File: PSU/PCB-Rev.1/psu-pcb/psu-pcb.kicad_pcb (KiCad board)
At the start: 2 copper layers, 100 x 100 mm, 60 parts, among them J1 Conn_02x07_Odd_Even, J2 OSTTC022162, J3 OSTTC022162, J4 OSTTC022162, J5 OSTTC022162, J6 OSTTC022162, J7 OSTTC022162, J8 Conn_02x05_Odd_Even, Q1 2N7002, Q2 2N7002, Q3 2N7002, Q4 FQP27P06, Q5 2N7002, U1 PIC12F1501-IP, U2 ADS1110

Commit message: psu ready to be validated
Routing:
- net +12V: track 135.8 -> 119.2 mm
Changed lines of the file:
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@@
-(kicad_pcb (version 20171130) (host pcbnew 5.0.2+dfsg1-1~bpo9+1)
+(kicad_pcb (version 20171130) (host pcbnew "(5.1.5)-3")
   (general
     (thickness 1.6)
     (drawings 6)
-    (tracks 213)
+    (tracks 211)
     (zones 0)
     (modules 60)
@@
     (38 B.Mask user)
     (39 F.Mask user)
-    (40 Dwgs.User user)
-    (41 Cmts.User user)
-    (42 Eco1.User user)
-    (43 Eco2.User user)
+    (40 Dwgs.User user hide)
+    (41 Cmts.User user hide)
+    (42 Eco1.User user hide)
+    (43 Eco2.User user hide)
     (44 Edge.Cuts user)
     (45 Margin user)
     (46 B.CrtYd user)
     (47 F.CrtYd user)
-    (48 B.Fab user)
-    (49 F.Fab user)
+    (48 B.Fab user hide)
+    (49 F.Fab user hide)
   )
   (setup
-    (last_trace_width 0.25)
+    (last_trace_width 2.54)
     (user_trace_width 1.27)
     (user_trace_width 2.54)
@@
     (zone_45_only no)
     (trace_min 0.2)
-    (segment_width 0.2)
-    (edge_width 0.15)
     (via_size 0.8)
     (via_drill 0.4)
@@
     (uvia_min_size 0.2)
     (uvia_min_drill 0.1)
+    (edge_width 0.15)
+    (segment_width 0.2)
     (pcb_text_width 0.3)
     (pcb_text_size 1.5 1.5)
@@
     (solder_mask_min_width 0.25)
     (aux_axis_origin 0 0)
-    (visible_elements FFFFFF7F)
+    (visible_elements 7FFFFFFF)
     (pcbplotparams
       (layerselection 0x010fc_ffffffff)
@@
   (gr_line (start 120 120) (end 120 20) (layer Edge.Cuts) (width 0.01))
   (gr_line (start 20 20) (end 20 120) (layer Edge.Cuts) (width 0.01))
-  (via (at 116.84 22.86) (size 3.81) (drill 2.54) (layers F.Cu B.Cu) (net 2))
-  (via (at 36.83 83.185) (size 0.8) (drill 0.4) (layers F.Cu B.Cu) (net 2))
-  (via (at 42.545 53.34) (size 0.8) (drill 0.4) (layers F.Cu B.Cu) (net 2))
   (segment (start 38.735 33.655) (end 34.925 29.845) (width 2.54) (layer F.Cu) (net 1))
   (segment (start 41.275 33.655) (end 38.735 33.655) (width 2.54) (layer F.Cu) (net 1))
   (segment (start 28.575 36.195) (end 34.925 29.845) (width 2.54) (layer B.Cu) (net 1))
   (segment (start 26.035 36.195) (end 28.575 36.195) (width 2.54) (layer B.Cu) (net 1))
+  (via (at 116.84 22.86) (size 3.81) (drill 2.54) (layers F.Cu B.Cu) (net 2))
+  (via (at 36.83 83.185) (size 0.8) (drill 0.4) (layers F.Cu B.Cu) (net 2))
+  (via (at 42.545 53.34) (size 0.8) (drill 0.4) (layers F.Cu B.Cu) (net 2))
   (segment (start 66.04 36.8) (end 66.04 35.56) (width 0.25) (layer F.Cu) (net 2))
   (segment (start 62.865 39.975) (end 66.04 36.8) (width 0.25) (layer F.Cu) (net 2))
@@
   (segment (start 63.915 55.025) (end 63.5 54.61) (width 0.25) (layer F.Cu) (net 8))
   (segment (start 63.915 60.96) (end 63.915 55.025) (width 0.25) (layer F.Cu) (net 8))
-  (segment (start 68.780001 76.079999) (end 69.93 74.93) (width 6.35) (layer B.Cu) (net 9))
-  (segment (start 62.865 81.995) (end 68.780001 76.079999) (width 6.35) (layer B.Cu) (net 9))
-  (segment (start 62.865 91.36) (end 62.865 81.995) (width 6.35) (layer B.Cu) (net 9))
-  (segment (start 65.485 93.98) (end 62.865 91.36) (width 6.35) (layer B.Cu) (net 9))
-  (segment (start 69.93 74.93) (end 54.69 59.69) (width 6.35) (layer B.Cu) (net 9))
   (segment (start 44.875 28.745) (end 47.625 25.995) (width 2.54) (layer F.Cu) (net 9))
   (segment (start 44.875 33.655) (end 44.875 28.745) (width 2.54) (layer F.Cu) (net 9))
@@
   (segment (start 64.135 52.705) (end 66.04 54.61) (width 0.25) (layer F.Cu) (net 9))
   (segment (start 59.055 52.705) (end 64.135 52.705) (width 0.25) (layer F.Cu) (net 9))
-  (segment (start 63.701002 50.165) (end 54.69 50.165) (width 2.54) (layer B.Cu) (net 9))
-  (segment (start 66.04 52.503998) (end 63.701002 50.165) (width 2.54) (layer B.Cu) (net 9))
-  (segment (start 66.04 54.61) (end 66.04 52.503998) (width 2.54) (layer B.Cu) (net 9))
-  (segment (start 54.69 59.69) (end 54.69 50.165) (width 6.35) (layer B.Cu) (net 9))
-  (segment (start 54.69 50.165) (end 54.69 25.4) (width 6.35) (layer B.Cu) (net 9))
+  (segment (start 66.04 36.75) (end 66.04 54.61) (width 2.54) (layer B.Cu) (net 9))
+  (segment (start 54.69 25.4) (end 66.04 36.75) (width 2.54) (layer B.Cu) (net 9))
+  (segment (start 66.04 71.04) (end 69.93 74.93) (width 2.54) (layer B.Cu) (net 9))
+  (segment (start 66.04 54.61) (end 66.04 71.04) (width 2.54) (layer B.Cu) (net 9))
+  (segment (start 65.445 79.415) (end 65.445 83.185) (width 2.54) (layer B.Cu) (net 9))
+  (segment (start 69.93 74.93) (end 65.445 79.415) (width 2.54) (layer B.Cu) (net 9))
+  (segment (start 65.445 93.94) (end 65.485 93.98) (width 2.54) (layer B.Cu) (net 9))
+  (segment (start 65.445 83.185) (end 65.445 93.94) (width 2.54) (layer B.Cu) (net 9))
   (segment (start 83.265 54.61) (end 76.835 54.61) (width 2.54) (layer F.Cu) (net 10))
   (segment (start 83.9 55.245) (end 83.265 54.61) (width 2.54) (layer F.Cu) (net 10))

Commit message: update
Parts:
- added G***: LOGO, cidco:logo cidco, F.Cu at (48.3, 78.1)
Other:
- board text removed: "CIDCO.CA Poseidon PSU"

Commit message: update psu and hat
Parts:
- moved R14 31.4 mm to (89.2, 57.1)
- moved Q5 29.8 mm to (92.7, 61.0)
- moved R15 29.7 mm to (96.2, 57.8), turned to 180 degrees
- moved Q4 29.2 mm to (92.7, 53.3)
- moved R11 26.7 mm to (79.4, 59.7), turned to 90 degrees
- moved Q1 26.1 mm to (83.2, 61.6)
- moved C12 11.6 mm to (85.1, 53.3), turned to 90 degrees
- moved L4 11.0 mm to (75.6, 53.3)
- moved C11 10.9 mm to (66.0, 53.4)
- moved J7 6.38 mm to (61.6, 108.0)
- moved G*** 4.58 mm to (45.7, 81.9)
- moved C1 4.45 mm to (52.1, 43.5)
- moved D1 4.45 mm to (39.4, 29.8)
- moved D2 4.45 mm to (55.9, 37.2)
- moved F1 4.45 mm to (47.5, 33.7)
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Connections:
- C11 pad 1: Net-(C11-Pad1) -> +12V
- D3 pad 1: Net-(C12-Pad1) -> Net-(D3-Pad1)
- J4 pad 2: Net-(C12-Pad1) -> Net-(D3-Pad1)
- J8 pad 10: Net-(J8-Pad10) -> (no net)
- J8 pad 2: Net-(J8-Pad2) -> (no net)
- J8 pad 4: Net-(J8-Pad4) -> (no net)
- J8 pad 6: Net-(J8-Pad6) -> (no net)
- J8 pad 8: Net-(J8-Pad8) -> (no net)
- L4 pad 2: Net-(C11-Pad1) -> +12V
- Q4 pad 2: +12V -> Net-(C12-Pad1)
- Q4 pad 3: Net-(C11-Pad1) -> Net-(D3-Pad1)
- R14 pad 1: +12V -> Net-(C12-Pad1)
- R15 pad 1: +12V -> Net-(C12-Pad1)
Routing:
- net GND: track 28.6 -> 51.7 mm, vias 8 -> 7
- net Net-(C11-Pad1): track 15.6 -> 0.00 mm
- net Net-(D3-Pad1): track 0.00 -> 13.5 mm
- net Net-(C12-Pad1): track 24.7 -> 32.8 mm
- net 5v_on: track 61.9 -> 55.0 mm
- net Net-(C5-Pad1): track 54.9 -> 52.4 mm
- net SDA: track 47.7 -> 50.2 mm
- net Net-(D1-Pad1): track 19.4 -> 21.9 mm
- net +12V: track 119.2 -> 121.3 mm
- net read_sw: track 35.9 -> 33.9 mm
- net SCK: track 44.3 -> 46.1 mm
- net Net-(PS1-Pad1): track 9.57 -> 7.97 mm
- net 12v_on: track 71.7 -> 73.2 mm, vias 0 -> 1
- net Net-(PS1-Pad5): track 26.2 -> 24.9 mm
- net +5V: track 151.6 -> 150.6 mm
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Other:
- board text added: "+ -"
- board text added: "12V IN"
- board text added: "12V OUT"
- board text added: "24V OUT"
- board text added: "3.3V OUT"
- board text added: "5V OUT"
- board text added: "DD20200127 Rev. 1.0"
- board text added: "Hydro B. HAT"
- board text added: "Hydro B. PSU"
- board text added: "ICSP"
- board text added: "Read Switch"
- board text removed: "DD200127 Rev. 1.0"

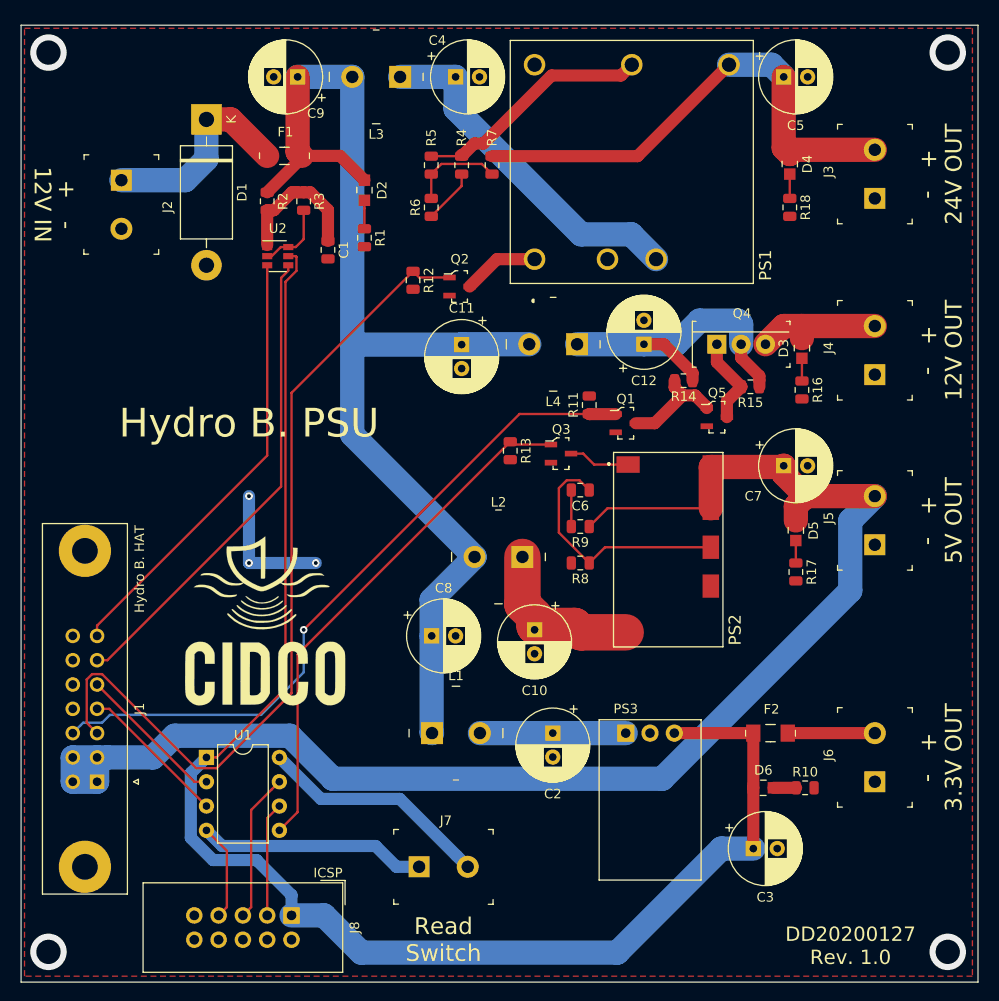
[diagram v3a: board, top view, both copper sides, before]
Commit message: smt to TH
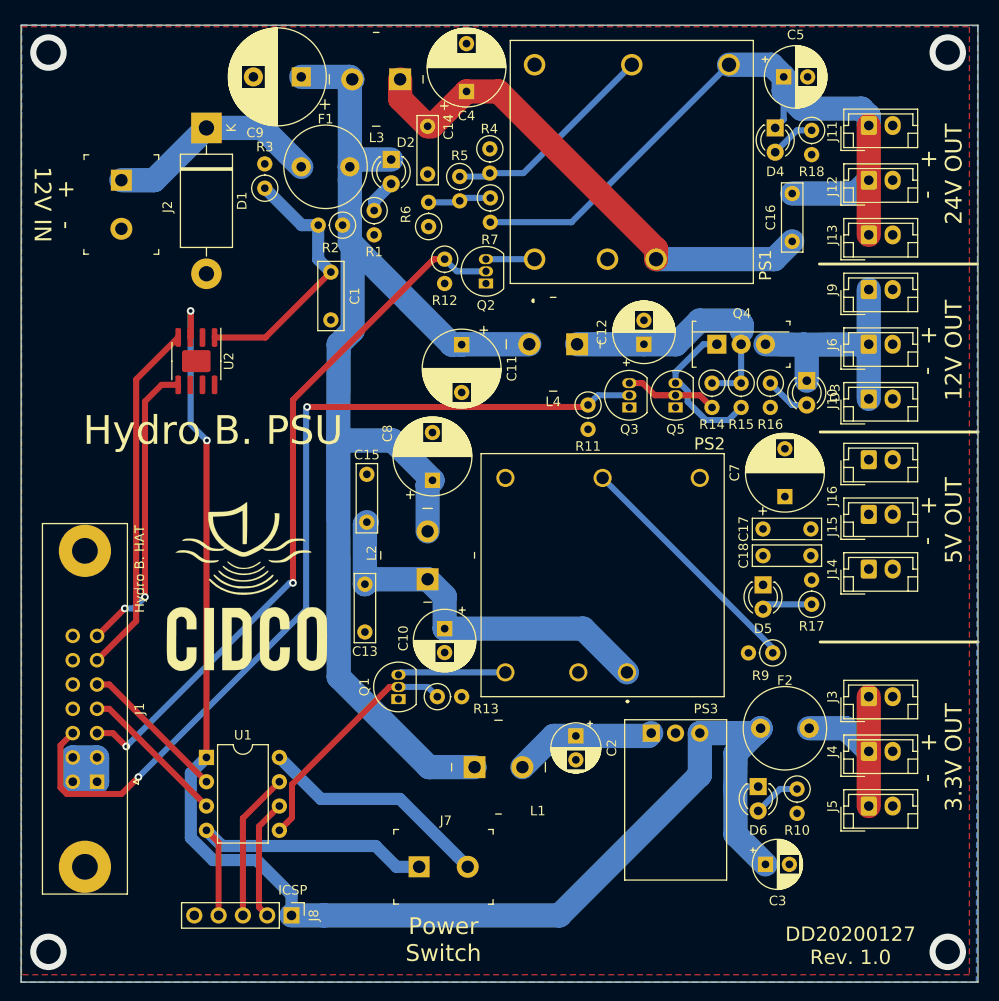
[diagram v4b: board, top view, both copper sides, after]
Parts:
- removed C6: C, Capacitor_SMD:C_0805_2012Metric
- removed R8: R_US, Resistor_SMD:R_0805_2012Metric
- added C13: 10UF, Capacitor_THT:C_Rect_L7.0mm_W2.0mm_P5.00mm, F.Cu at (55.9, 78.4)
- added C14: 4.7UF 50V, Capacitor_THT:C_Rect_L7.0mm_W2.0mm_P5.00mm, F.Cu at (62.5, 30.6)
- added C15: 0.1UF, Capacitor_THT:C_Rect_L7.0mm_W2.0mm_P5.00mm, F.Cu at (56.1, 71.9)
- added C16: 1NF 2KV, Capacitor_THT:C_Rect_L7.0mm_W2.0mm_P5.00mm, F.Cu at (100.6, 42.6)
- added C17: 10UF, Capacitor_THT:C_Rect_L7.0mm_W2.0mm_P5.00mm, F.Cu at (97.5, 72.6)
- added C18: 0.1UF, Capacitor_THT:C_Rect_L7.0mm_W2.0mm_P5.00mm, F.Cu at (97.5, 75.4)
- added J10: Conn_01x02, Connector_JST:JST_EH_B2B-EH-A_1x02_P2.50mm_Vertical, F.Cu at (108.6, 59.1)
- added J11: Conn_01x02, Connector_JST:JST_EH_B2B-EH-A_1x02_P2.50mm_Vertical, F.Cu at (108.6, 30.5)
- added J12: Conn_01x02, Connector_JST:JST_EH_B2B-EH-A_1x02_P2.50mm_Vertical, F.Cu at (108.6, 36.2)
- added J13: Conn_01x02, Connector_JST:JST_EH_B2B-EH-A_1x02_P2.50mm_Vertical, F.Cu at (108.6, 41.9)
- added J14: Conn_01x02, Connector_JST:JST_EH_B2B-EH-A_1x02_P2.50mm_Vertical, F.Cu at (108.6, 76.8)
- added J15: Conn_01x02, Connector_JST:JST_EH_B2B-EH-A_1x02_P2.50mm_Vertical, F.Cu at (108.6, 71.1)
- added J16: Conn_01x02, Connector_JST:JST_EH_B2B-EH-A_1x02_P2.50mm_Vertical, F.Cu at (108.6, 65.4)
- added J9: Conn_01x02, Connector_JST:JST_EH_B2B-EH-A_1x02_P2.50mm_Vertical, F.Cu at (108.6, 47.6)
- C1: value C -> 0.1u; footprint Capacitor_SMD:C_0805_2012Metric -> Capacitor_THT:C_Rect_L7.0mm_W2.5mm_P5.00mm
- C10: value CP1 -> 47UF 35V; footprint Capacitor_THT:CP_Radial_D7.5mm_P2.50mm -> Capacitor_THT:CP_Radial_D6.3mm_P2.50mm
- C11, C4: value CP1 -> 100UF 50V; footprint Capacitor_THT:CP_Radial_D7.5mm_P2.50mm -> Capacitor_THT:CP_Radial_D8.0mm_P5.00mm
- C12, C5: value CP1 -> 47UF 50V; footprint Capacitor_THT:CP_Radial_D7.5mm_P2.50mm -> Capacitor_THT:CP_Radial_D6.3mm_P2.50mm
- C2: value CP1 -> 10u 35v; footprint Capacitor_THT:CP_Radial_D7.5mm_P2.50mm -> Capacitor_THT:CP_Radial_D5.0mm_P2.50mm
- C3: value CP1 -> 10u 10v; footprint Capacitor_THT:CP_Radial_D7.5mm_P2.50mm -> Capacitor_THT:CP_Radial_D5.0mm_P2.50mm
- C7: value CP1 -> 330uf 16v; footprint Capacitor_THT:CP_Radial_D7.5mm_P2.50mm -> Capacitor_THT:CP_Radial_D8.0mm_P5.00mm
- C8: value CP1 -> 100UF 35V; footprint Capacitor_THT:CP_Radial_D7.5mm_P2.50mm -> Capacitor_THT:CP_Radial_D8.0mm_P5.00mm
- C9: value CP1 -> 330UF 50V; footprint Capacitor_THT:CP_Radial_D7.5mm_P2.50mm -> Capacitor_THT:CP_Radial_D10.0mm_P5.00mm
- D2, D3, D4, D5, D6: footprint digikey-footprints:0805 -> LED_THT:LED_D3.0mm_Clear
- F1, F2: footprint digikey-footprints:1206 -> Fuse:Fuse_Littelfuse_372_D8.50mm
- J3, J4, J5, J6: value OSTTC022162 -> Conn_01x02; footprint digikey-footprints:Term_Block_1x2_P5.08MM -> Connector_JST:JST_EH_B2B-EH-A_1x02_P2.50mm_Vertical
- J8: value Conn_02x05_Odd_Even -> Conn_01x05; footprint Connector_IDC:IDC-Header_2x05_P2.54mm_Vertical -> Connector_PinHeader_2.54mm:PinHeader_1x05_P2.54mm_Vertical
- L1: value 13R106C -> 1uh
- L3: value 13R106C -> 2.2UH 4A
- L4: value 13R106C -> 1UH
- PS2: value APXW005A0X3-SRZ -> SKMW30F-05; footprint APXW005A0X3SRZ -> SKMW30G-12:SKMW30G12
- Q1, Q2, Q3, Q5: value 2N7002 -> 2N7000; footprint digikey-footprints:SOT-23-3 -> Package_TO_SOT_THT:TO-92_Inline
- R1, R14, R15: value R_US -> 10k; footprint Resistor_SMD:R_0805_2012Metric -> Resistor_THT:R_Axial_DIN0207_L6.3mm_D2.5mm_P2.54mm_Vertical
- R10: value R_US -> 220; footprint Resistor_SMD:R_0805_2012Metric -> Resistor_THT:R_Axial_DIN0207_L6.3mm_D2.5mm_P2.54mm_Vertical
- R11, R12, R13: value R_US -> 1k; footprint Resistor_SMD:R_0805_2012Metric -> Resistor_THT:R_Axial_DIN0207_L6.3mm_D2.5mm_P2.54mm_Vertical
- R16: value R_US -> 2k; footprint Resistor_SMD:R_0805_2012Metric -> Resistor_THT:R_Axial_DIN0207_L6.3mm_D2.5mm_P2.54mm_Vertical
- R17: value R_US -> 560; footprint Resistor_SMD:R_0805_2012Metric -> Resistor_THT:R_Axial_DIN0207_L6.3mm_D2.5mm_P2.54mm_Vertical
- R18: value R_US -> 3.9k; footprint Resistor_SMD:R_0805_2012Metric -> Resistor_THT:R_Axial_DIN0207_L6.3mm_D2.5mm_P2.54mm_Vertical
- R2: value R_US -> 7.87k 0.1%; footprint Resistor_SMD:R_0805_2012Metric -> Resistor_THT:R_Axial_DIN0207_L6.3mm_D2.5mm_P2.54mm_Vertical
- R3: value R_US -> 1.27k 0.1%; footprint Resistor_SMD:R_0805_2012Metric -> Resistor_THT:R_Axial_DIN0207_L6.3mm_D2.5mm_P2.54mm_Vertical
- R4: value R_US -> XX; footprint Resistor_SMD:R_0805_2012Metric -> Resistor_THT:R_Axial_DIN0207_L6.3mm_D2.5mm_P2.54mm_Vertical
- R5: value R_US -> 20K; footprint Resistor_SMD:R_0805_2012Metric -> Resistor_THT:R_Axial_DIN0207_L6.3mm_D2.5mm_P2.54mm_Vertical
- R6: value R_US -> 2.87K; footprint Resistor_SMD:R_0805_2012Metric -> Resistor_THT:R_Axial_DIN0207_L6.3mm_D2.5mm_P2.54mm_Vertical
- R7: value R_US -> 24.872K; footprint Resistor_SMD:R_0805_2012Metric -> Resistor_THT:R_Axial_DIN0207_L6.3mm_D2.5mm_P2.54mm_Vertical
- R9: value R_US -> xx; footprint Resistor_SMD:R_0805_2012Metric -> Resistor_THT:R_Axial_DIN0207_L6.3mm_D2.5mm_P2.54mm_Vertical
- U2: value ADS1110 -> MCP3426-xSN; footprint Package_TO_SOT_SMD:SOT-23-6 -> Package_SO:SOIC-8-1EP_3.9x4.9mm_P1.27mm_EP2.29x3mm
- moved J3 52.1 mm to (108.6, 90.2), turned to 0 degrees
- moved J6 45.7 mm to (108.6, 53.3), turned to 0 degrees
- moved J4 39.4 mm to (108.6, 95.9), turned to 0 degrees
- moved Q1 37.4 mm to (59.4, 90.4), turned to 90 degrees
- moved J5 27.3 mm to (108.6, 101.6), turned to 0 degrees
- moved R13 26.8 mm to (63.5, 90.2), turned to 0 degrees
- moved R9 24.1 mm to (98.6, 85.6)
- moved C8 16.3 mm to (63.0, 67.6), turned to 90 degrees
- moved U2 13.9 mm to (38.3, 55.1), turned to 270 degrees
- moved PS2 13.5 mm to (83.3, 87.6), turned to 0 degrees
- moved C10 9.40 mm to (64.3, 83.1)
- moved Q3 8.62 mm to (83.6, 59.9), turned to 90 degrees
- moved R18 8.37 mm to (102.6, 31.0)
- moved R2 8.26 mm to (53.6, 40.9), turned to 180 degrees
- moved L2 7.41 mm to (62.5, 75.4), turned to 90 degrees
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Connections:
- C5 pad 1: Net-(C5-Pad1) -> 24VOUT
- C7 pad 1: +5V -> 5VOUT
- D3 pad 1: Net-(D3-Pad1) -> 12VOUT
- D4 pad 1: Net-(C5-Pad1) -> 24VOUT
- D5 pad 1: +5V -> 5VOUT
- F2 pad 2: Net-(F2-Pad2) -> 3.3VOUT
- J1 pad 1: +5V -> 5VOUT
- J1 pad 2: +5V -> 5VOUT
- J1 pad 3: +5V -> 5VOUT
- J1 pad 4: +5V -> 5VOUT
- J3 pad 1: GND -> 3.3VOUT
- J3 pad 2: Net-(C5-Pad1) -> GND
- J4 pad 1: GND -> 3.3VOUT
- J4 pad 2: Net-(D3-Pad1) -> GND
- J5 pad 1: GND -> 3.3VOUT
- J5 pad 2: +5V -> GND
- J6 pad 1: GND -> 12VOUT
- J6 pad 2: Net-(F2-Pad2) -> GND
- J8 pad 2: (no net) -> ICSPCLK
- J8 pad 3: ICSPCLK -> ICSPDAT
- J8 pad 4: (no net) -> read_sw
- J8 pad 5: ICSPDAT -> GND
- PS1 pad 4: Net-(C5-Pad1) -> 24VOUT
- PS2 pad 1: Net-(PS2-Pad1) -> Net-(C10-Pad1)
- PS2 pad 2: Net-(C10-Pad1) -> GND
- PS2 pad 3: GND -> 5VOUT
- PS2 pad 4: Net-(C6-Pad1) -> Net-(PS2-Pad4)
- PS2 pad 5: +5V -> GND
- PS2 pad 6: +5V -> Net-(PS2-Pad6)
- Q1 pad 1: 12v_on -> GND
- Q1 pad 2: GND -> 5v_on
- Q1 pad 3: Net-(Q1-Pad3) -> Net-(PS2-Pad6)
- Q2 pad 1: 24v_on -> GND
- Q2 pad 2: GND -> 24v_on
- Q3 pad 1: 5v_on -> GND
- Q3 pad 2: GND -> 12v_on
- Q3 pad 3: Net-(PS2-Pad1) -> Net-(Q3-Pad3)
- Q4 pad 3: Net-(D3-Pad1) -> 12VOUT
- Q5 pad 1: Net-(Q1-Pad3) -> GND
- Q5 pad 2: GND -> Net-(Q3-Pad3)
- R14 pad 2: Net-(Q1-Pad3) -> Net-(Q3-Pad3)
- R7 pad 2: Net-(C5-Pad1) -> 24VOUT
- R9 pad 1: +5V -> Net-(PS2-Pad4)
- R9 pad 2: Net-(C6-Pad2) -> GND
- U2 pad 3: SCK -> +3V3
- U2 pad 5: +3V3 -> SCK
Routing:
- net +5V: track 150.6 -> 0.00 mm
- net 24VOUT: track 0.00 -> 76.2 mm
- net Net-(C5-Pad1): track 52.4 -> 0.00 mm
- net 5v_on: track 55.0 -> 25.2 mm
- net GND: track 51.7 -> 24.4 mm, vias 7 -> 4
- net Net-(C6-Pad1): track 26.5 -> 0.00 mm
- net 12VOUT: track 0.00 -> 26.2 mm
- net Net-(PS2-Pad4): track 0.00 -> 25.7 mm
- net Net-(C10-Pad1): track 17.5 -> 40.2 mm
- net 12v_on: track 73.2 -> 95.5 mm, vias 1 -> 2
- net 3.3VOUT: track 0.00 -> 18.7 mm
- net Net-(C14-Pad1): track 36.6 -> 54.5 mm
- net SCK: track 46.1 -> 31.3 mm, vias 0 -> 2
- net 24v_on: track 88.4 -> 74.0 mm, vias 0 -> 2
- net Net-(D3-Pad1): track 13.5 -> 0.00 mm
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- added copper zone on B.Cu, net 5VOUT
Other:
- board text added: "Power Switch"
- board text removed: "Read Switch"

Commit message: update
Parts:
- U2: footprint Package_SO:SOIC-8-1EP_3.9x4.9mm_P1.27mm_EP2.29x3mm -> Package_SO:SOIC-8_3.9x4.9mm_P1.27mm
- moved L1 9.58 mm to (76.8, 104.1)
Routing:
- net +12V: track 131.6 -> 141.3 mm
- net Net-(C2-Pad1): track 14.9 -> 18.9 mm
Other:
- board text added: "+12V IN-"
- board text removed: "12V IN"
